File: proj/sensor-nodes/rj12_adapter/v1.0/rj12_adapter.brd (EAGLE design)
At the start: 59 parts, among them J1 54602-908LF, J2 54602-908LF, U2 PCA9615DPJ, U3 MIC4680YM-TR, U4 LM2937IMP3.3NOPB, U5 APDS-9250, U7 TSL2591

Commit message: extracted design blocks from light controller
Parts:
- removed C2, C7: 0.1uF, openag-capacitors:C0603
- removed TP13, TP14, TP19, TP20, TP21, TP22, TP6, TP7: TPTP06R, openag-testpads:TP06R
- removed U5: APDS-9250, openag-sensors:APDS-9250
- removed U7: TSL2591, openag-sensors:DFN6_TAOS
- added J3, J4: OPENAG-I2C-RJ12, openag-connectors:OPENAG-I2C-RJ12
- added TP1, TP2, TP3, TP5: TPTP06R, openag-testpads:TP06R
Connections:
- new net IO: J4.2
- net +3V3: now also J3.5, J4.5, TP1.TP; no longer C2.1, C7.1, TP14.TP, TP21.TP, U5.3, U7.5
- net GND: now also J3.1, J4.1, TP5.TP; no longer C2.2, C7.2, TP13.TP, TP22.TP, U5.6, U7.3
- net SCL: now also J3.3, J4.3, TP3.TP; no longer TP20.TP, TP6.TP, U5.1, U7.1
- net SDA: now also J3.4, J4.4, TP2.TP; no longer TP19.TP, TP7.TP, U5.2, U7.6
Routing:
- net +3V3: track 305.8 -> 223.3 mm
- net SDA: track 116.1 -> 105.0 mm
- net SCL: track 113.3 -> 102.9 mm, vias 2 -> 0
- net GND: track 4.52 -> 3.23 mm, vias 10 -> 8
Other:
- board text added: "RJ12 Adapter v1.0"
- board text added: "RJ12-I2C Connector Pair"
- board text added: "RJ45 Connector w/dI2C Buffer, Chainable"
- board text removed: "0x29"
- board text removed: "0x52"
- board text removed: "APDS9250 Light Sensor"
- board text removed: "I2C Addr"
- board text removed: "Light Sensor Node v1.0"
- board text removed: "RJ45 Connector w/dI2C Buffer"
- board text removed: "TS2591 Light Sensor"

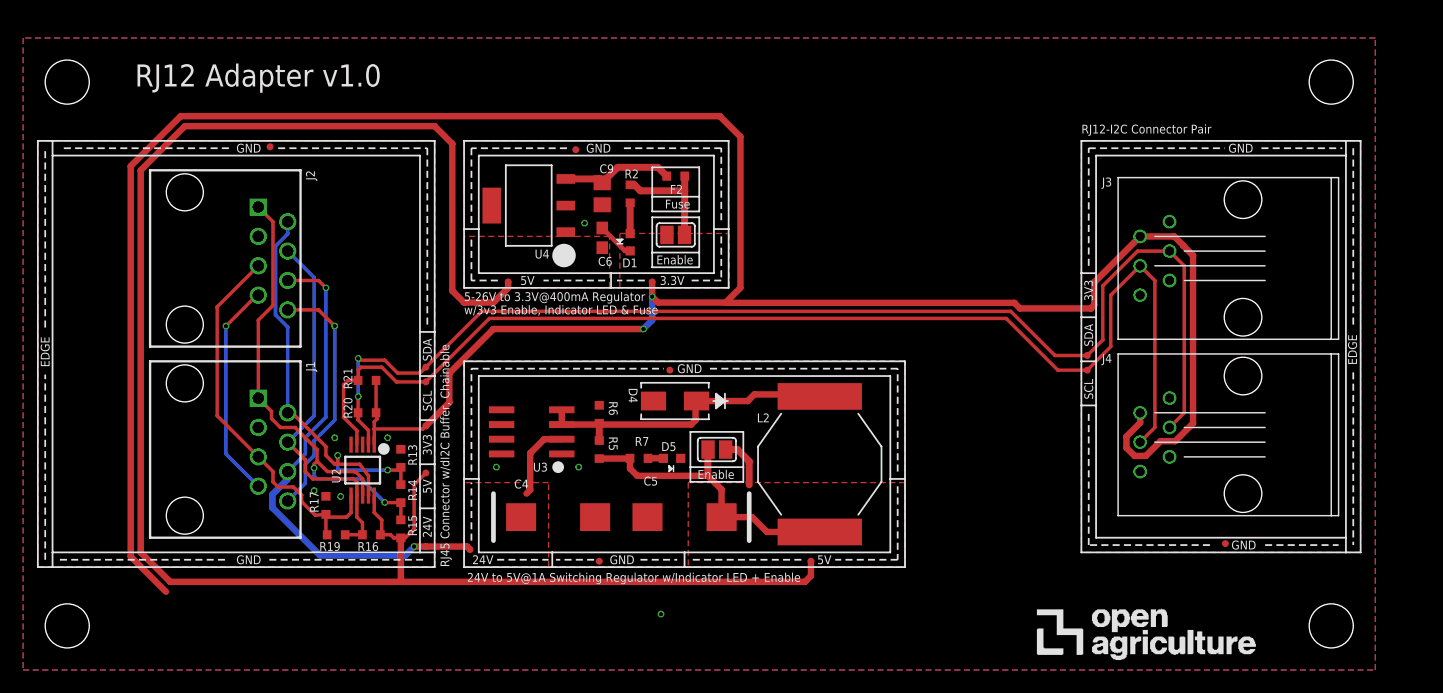
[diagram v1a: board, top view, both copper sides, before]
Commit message: added light and rj12 nodes, started working on light controller v2
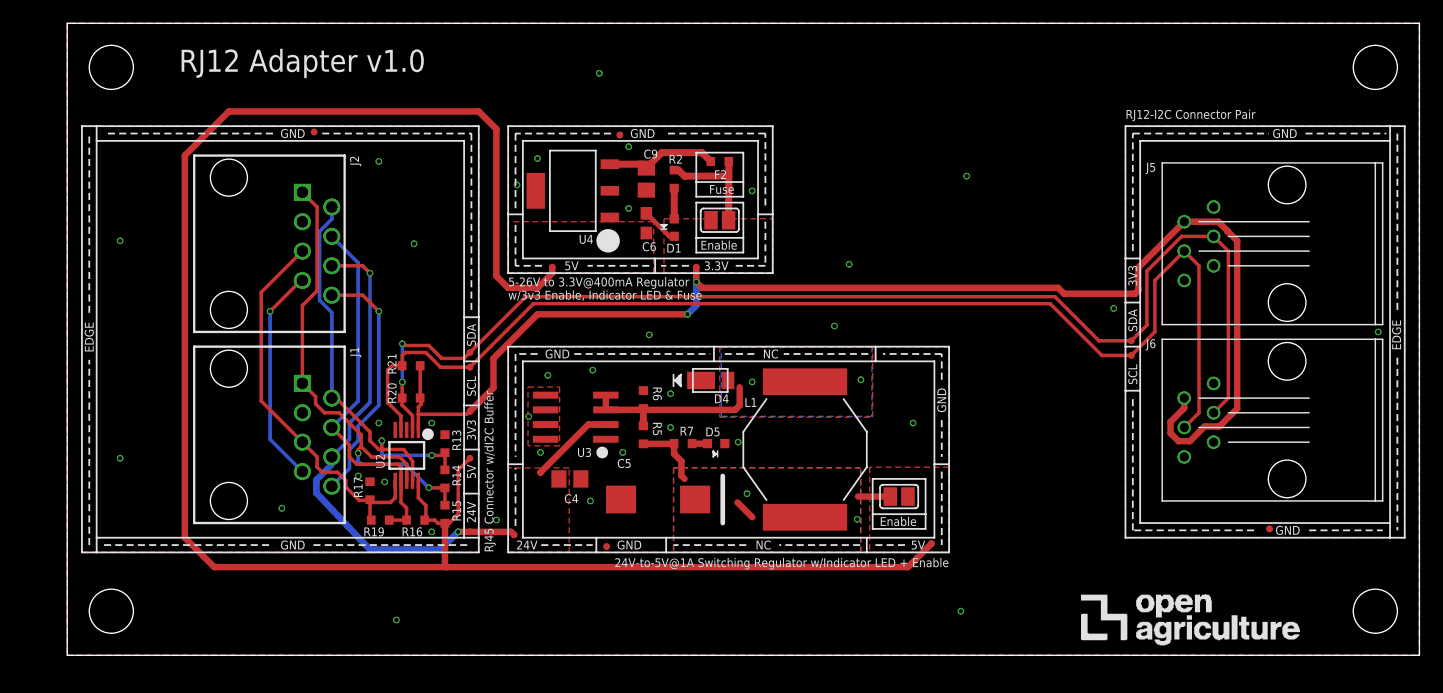
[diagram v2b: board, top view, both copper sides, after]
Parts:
- removed J3, J4: OPENAG-I2C-RJ12, openag-connectors:OPENAG-I2C-RJ12
- removed L2: 68uH, openag-inductors:UP2B
- removed SJ4: (no value), openag-connectors:SOLDERJUMPER_REFLOW_NOPASTE
- removed TP1, TP10, TP2, TP3, TP31: TPTP06R, openag-testpads:TP06R
- added J5, J6: OPENAG-I2C-RJ12, openag-connectors:OPENAG-I2C-RJ12
- added L1: 68uH, openag-inductors:UP2B
- added SJ2: (no value), openag-connectors:SOLDERJUMPER_REFLOW_NOPASTE
- added TP13, TP14, TP6, TP7: TPTP06R, openag-testpads:TP06R
- C4: device openag-capacitors:CT7343 -> openag-capacitors:C0805
- D4: value B260A-13-F -> SBR2A40P1-7; device openag-diodes:SMA -> openag-diodes:POWERDI123
- R13, R15, R16, R17: value NV -> 600
- R14, R19: value NV -> 120
- R2, R7: value 100 OHM -> 100
- R20, R21: value NV -> 10K
- moved TP12 59.6 mm to (91.9, 25.9), turned to 0 degrees
- moved TP11 40.7 mm to (92.3, 31.2), turned to 0 degrees
- moved TP5 25.4 mm to (74.7, 9.65), turned to 180 degrees
- moved FRAME1 24.1 mm to (77.2, 3.30), turned to 0 degrees
- moved D1 4.02 mm to (52.5, 37.0)
- moved R2 4.02 mm to (52.5, 41.1)
- moved U3 4.02 mm to (43.9, 20.6)
- moved TP34 4.02 mm to (34.8, 17.0)
- moved D5 4.02 mm to (56.1, 18.3)
- moved J2 4.02 mm to (14.0, 35.6)
- moved R13 4.02 mm to (32.6, 18.3)
- moved R14 4.02 mm to (32.6, 15.2)
- moved R15 4.02 mm to (32.6, 12.2)
- moved R5 4.02 mm to (49.8, 19.1)
- moved R6 4.02 mm to (49.8, 22.1)
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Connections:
- removed net TAB: U4.4
- net +24V: now also C4.1, TP7.TP; no longer C4.+, TP12.TP
- net +3V3: now also J5.5, J6.5, TP11.TP; no longer J3.5, J4.5, TP1.TP
- net +5V: now also SJ2.2, TP5.TP; no longer SJ4.2, TP10.TP
- net GND: now also C4.2, D4.-, J5.1, J6.1, TP13.TP, TP6.TP, U4.4; no longer C4.-, D4.2, J3.1, J4.1, TP11.TP, TP31.TP, TP5.TP
- net IO: now also J6.2; no longer J4.2
- net N$31: now also D4.+, L1.1; no longer D4.1, L2.1
- net N$33: now also L1.2, SJ2.1; no longer L2.2, SJ4.1
- net SCL: now also J5.3, J6.3, TP12.TP; no longer J3.3, J4.3, TP3.TP
- net SDA: now also J5.4, J6.4, TP14.TP; no longer J3.4, J4.4, TP2.TP
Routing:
- net +3V3: track 223.3 -> 115.2 mm
- net N$33: track 25.9 -> 10.7 mm, vias 0 -> 2
- net N$31: track 27.3 -> 16.2 mm, vias 0 -> 2
- net +5V: track 162.2 -> 163.7 mm
- net +24V: track 50.5 -> 51.8 mm
- net GND: vias 8 -> 35
- added copper zone on layer 1, net N$31
- added copper zone on layer 16, net N$31
- added copper zone on layer 1, net N$33
- added copper zone on layer 16, net N$33
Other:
- board outline added: 116.8 x 54.6 mm
- board text added: "24V-to-5V@1A Switching Regulator w/Indicator LED + Enable"
- board text added: "NC"
- board text added: "RJ45 Connector w/dI2C Buffer"
- board text removed: "24V to 5V@1A Switching Regulator w/Indicator LED + Enable"
- board text removed: "RJ45 Connector w/dI2C Buffer, Chainable"
